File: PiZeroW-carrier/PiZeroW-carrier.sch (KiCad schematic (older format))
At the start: 0 parts

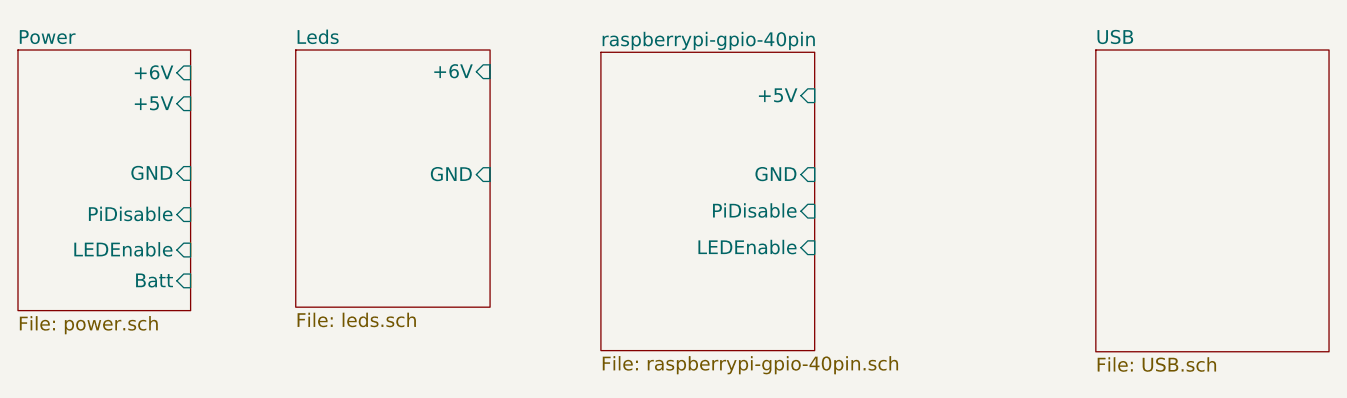
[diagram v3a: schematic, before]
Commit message: Before Trace fix of LED AND PIDISABLE
Push before tracing fix of LEDEnable and PIDisable
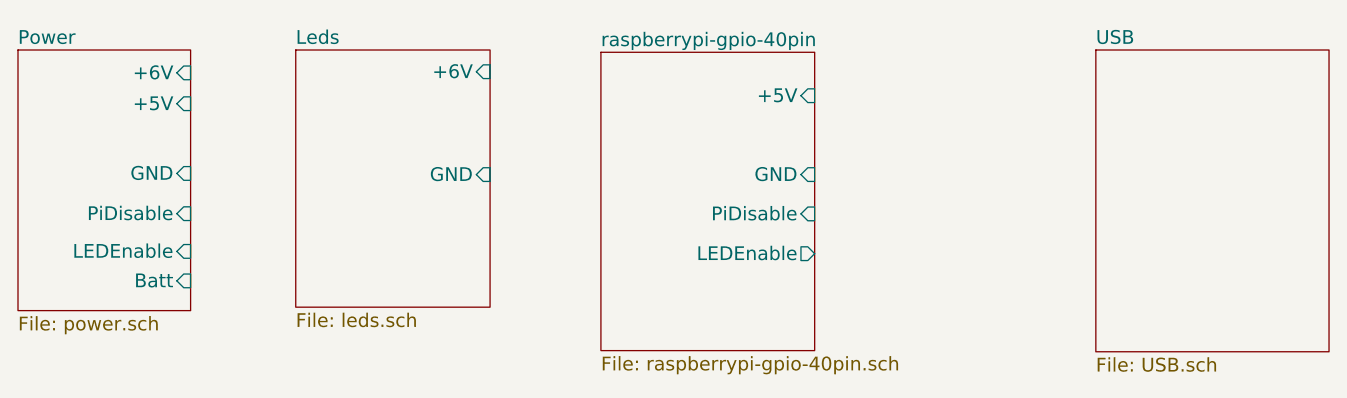
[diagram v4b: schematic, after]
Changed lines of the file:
@@
 F4 "+6V" I R 1900 1300 60
 F5 "+5V" I R 1900 1435 60
-F6 "PiDisable" I R 1900 1920 60
-F7 "LEDEnable" I R 1900 2075 60
+F6 "LEDEnable" I R 1900 2081 60
+F7 "PiDisable" I R 1900 1916 60
 $EndSheet
 $Sheet
@@
 F2 "+5V" I R 4630 1400 60
 F3 "GND" I R 4630 1745 60
-F4 "LEDEnable" I R 4630 2065 60
-F5 "PiDisable" I R 4630 1905 60
+F4 "PiDisable" I R 4630 1917 60
+F5 "LEDEnable" O R 4630 2091 60
 $EndSheet
 $Sheet

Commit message: Re Arranged PCB with hole for camera.
PCB re arranged to allow more room for camera and Barrel Jack
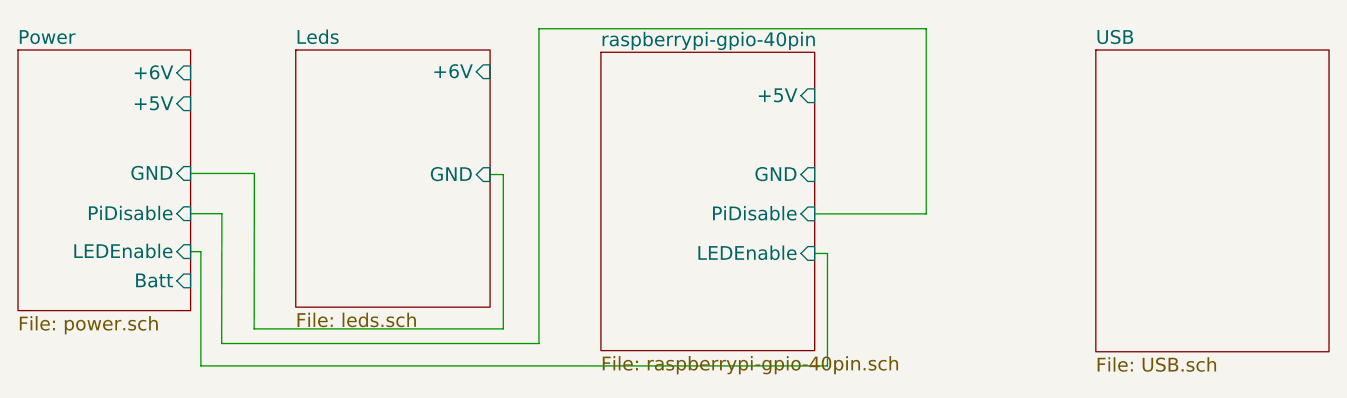
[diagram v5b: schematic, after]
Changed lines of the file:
@@
 F4 "+6V" I R 1900 1300 60
 F5 "+5V" I R 1900 1435 60
-F6 "LEDEnable" I R 1900 2081 60
+F6 "LEDEnable" I R 1900 2082 60
 F7 "PiDisable" I R 1900 1916 60
 $EndSheet
@@
 F3 "GND" I R 4630 1745 60
 F4 "PiDisable" I R 4630 1917 60
-F5 "LEDEnable" O R 4630 2091 60
+F5 "LEDEnable" I R 4630 2090 60
 $EndSheet
 $Sheet
@@
 F1 "USB.sch" 60
 $EndSheet
+Wire Wire Line
+	1900 1740 2179 1740
+Wire Wire Line
+	2179 1740 2178 2420
+Wire Wire Line
+	2178 2420 3268 2420
+Wire Wire Line
+	3268 2420 3268 1745
+Wire Wire Line
+	3268 1745 3210 1745
+Wire Wire Line
+	4630 2090 4686 2090
+Wire Wire Line
+	4686 2090 4686 2582
+Wire Wire Line
+	4686 2582 1945 2582
+Wire Wire Line
+	1945 2582 1945 2082
+Wire Wire Line
+	1945 2082 1900 2082
+Wire Wire Line
+	4630 1917 5118 1917
+Wire Wire Line
+	5118 1917 5118 1107
+Wire Wire Line
+	5118 1107 3424 1107
+Wire Wire Line
+	3424 1107 3424 2484
+Wire Wire Line
+	3424 2484 2036 2484
+Wire Wire Line
+	2036 2484 2037 1916
+Wire Wire Line
+	2037 1916 1900 1916
 $EndSCHEMATC

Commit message: Fix of Copper Pour and Placement of the Barrel Jack
Fixed the Copper Pour from the last Push and Re positioned the Barrel Jack
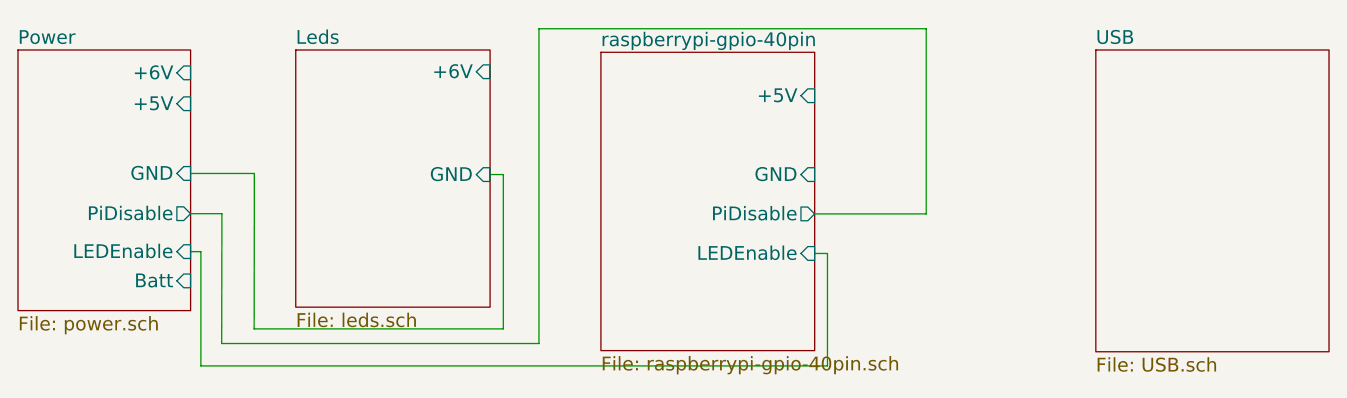
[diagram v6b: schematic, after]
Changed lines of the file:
@@
 F5 "+5V" I R 1900 1435 60
 F6 "LEDEnable" I R 1900 2082 60
-F7 "PiDisable" I R 1900 1916 60
+F7 "PiDisable" O R 1900 1916 60
 $EndSheet
 $Sheet
@@
 F2 "+5V" I R 4630 1400 60
 F3 "GND" I R 4630 1745 60
-F4 "PiDisable" I R 4630 1917 60
+F4 "PiDisable" O R 4630 1917 60
 F5 "LEDEnable" I R 4630 2090 60
 $EndSheet

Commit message: Layout Change
Layout Change #2
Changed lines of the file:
@@
 F4 "+6V" I R 1900 1300 60
 F5 "+5V" I R 1900 1435 60
-F6 "LEDEnable" I R 1900 2082 60
+F6 "LEDEnable" O R 1900 2082 60
 F7 "PiDisable" O R 1900 1916 60
 $EndSheet
@@
 F3 "GND" I R 4630 1745 60
 F4 "PiDisable" O R 4630 1917 60
-F5 "LEDEnable" I R 4630 2090 60
+F5 "LEDEnable" O R 4630 2090 60
 $EndSheet
 $Sheet

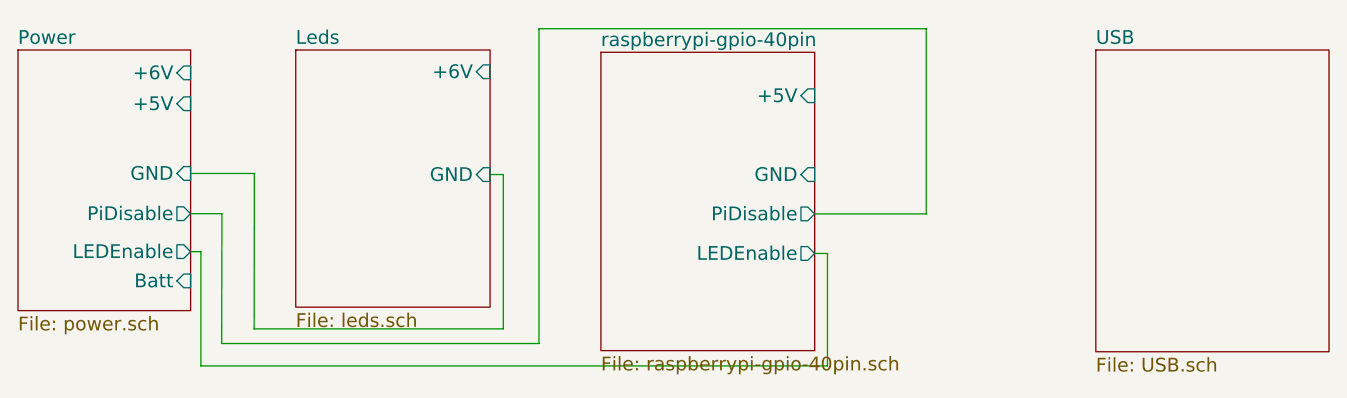
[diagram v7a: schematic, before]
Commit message: PCb Now with PIDisable and 6V Connection.
Featuring a PCB With proper PIDisable and 6V Connections
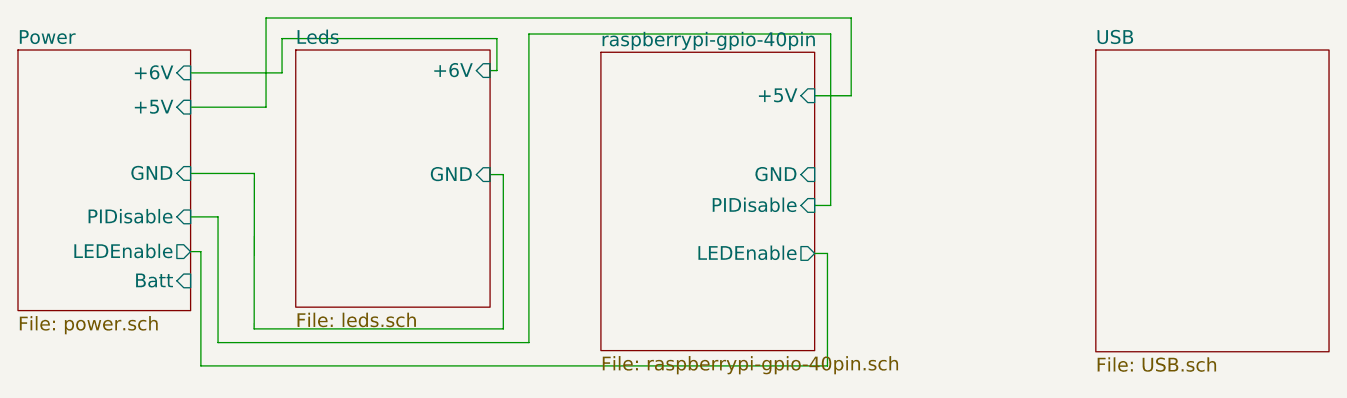
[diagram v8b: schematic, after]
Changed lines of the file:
@@
 F3 "GND" I R 1900 1740 60
 F4 "+6V" I R 1900 1300 60
-F5 "+5V" I R 1900 1435 60
+F5 "+5V" I R 1900 1450 60
 F6 "LEDEnable" O R 1900 2082 60
-F7 "PiDisable" O R 1900 1916 60
+F7 "PIDisable" I R 1900 1930 60
 $EndSheet
 $Sheet
@@
 F0 "Leds" 60
 F1 "leds.sch" 60
-F2 "+6V" I R 3210 1295 60
+F2 "+6V" I R 3210 1290 60
 F3 "GND" I R 3210 1745 60
 $EndSheet
@@
 F2 "+5V" I R 4630 1400 60
 F3 "GND" I R 4630 1745 60
-F4 "PiDisable" O R 4630 1917 60
-F5 "LEDEnable" O R 4630 2090 60
+F4 "LEDEnable" O R 4630 2090 60
+F5 "PIDisable" I R 4630 1880 60
 $EndSheet
 $Sheet
@@
 	1945 2082 1900 2082
 Wire Wire Line
-	4630 1917 5118 1917
+	4630 1880 4700 1880
 Wire Wire Line
-	5118 1917 5118 1107
+	4700 1880 4700 1130
 Wire Wire Line
-	5118 1107 3424 1107
+	4700 1130 3380 1130
 Wire Wire Line
-	3424 1107 3424 2484
+	3380 1130 3380 2480
 Wire Wire Line
-	3424 2484 2036 2484
+	3380 2480 2020 2480
 Wire Wire Line
-	2036 2484 2037 1916
+	2020 2480 2020 1930
 Wire Wire Line
-	2037 1916 1900 1916
+	2020 1930 1900 1930
+Wire Wire Line
+	1900 1300 2300 1300
+Wire Wire Line
+	2300 1300 2300 1150
+Wire Wire Line
+	2300 1150 3240 1150
+Wire Wire Line
+	3240 1150 3240 1290
+Wire Wire Line
+	3240 1290 3210 1290
+Wire Wire Line
+	1900 1450 2230 1450
+Wire Wire Line
+	2230 1450 2230 1060
+Wire Wire Line
+	2230 1060 4790 1060
+Wire Wire Line
+	4790 1060 4790 1400
+Wire Wire Line
+	4790 1400 4630 1400
 $EndSCHEMATC
